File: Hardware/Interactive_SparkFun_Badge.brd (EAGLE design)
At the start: 88.9 x 63.5 mm, 27 parts, among them J1 AVR_SPI_PRG_6NS, U1 ATMEGA328P, Y1 8MHZ

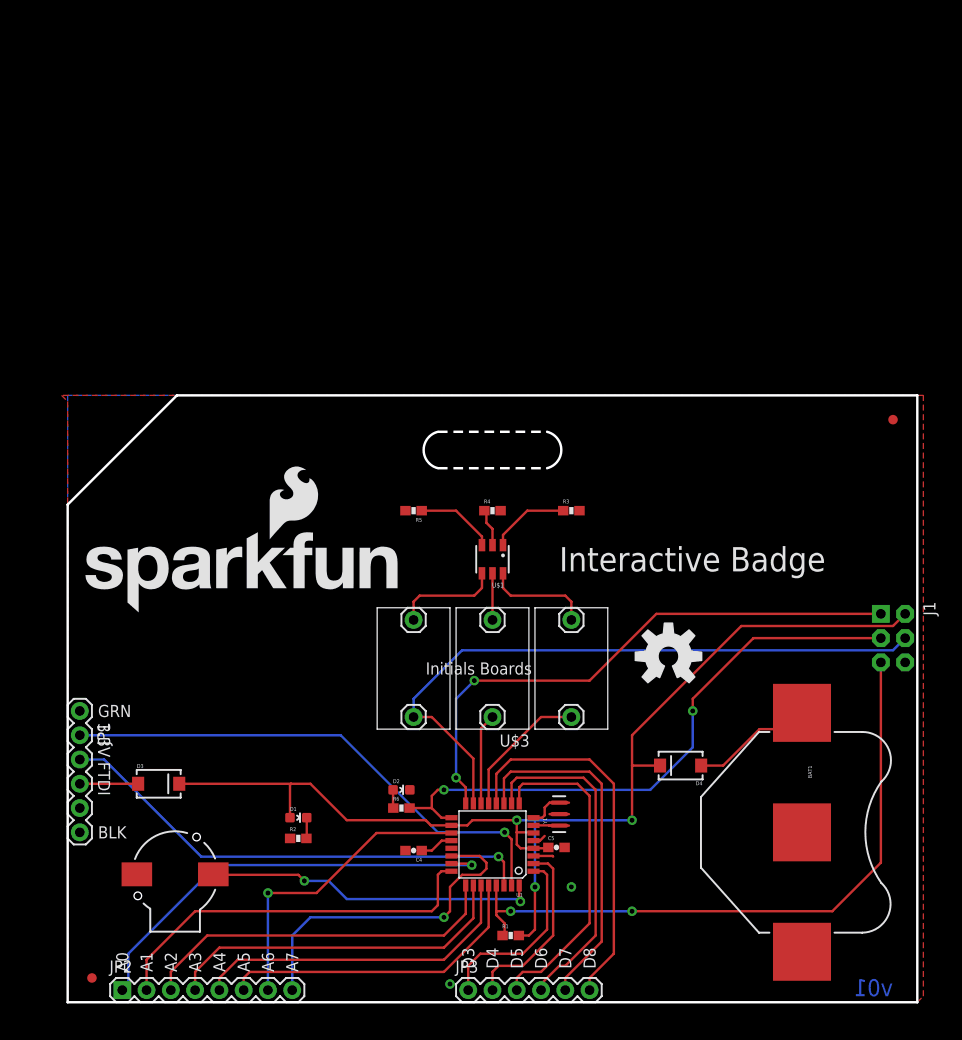
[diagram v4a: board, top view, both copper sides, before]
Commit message: Updating to round corners, zener diodes, larger letter boards
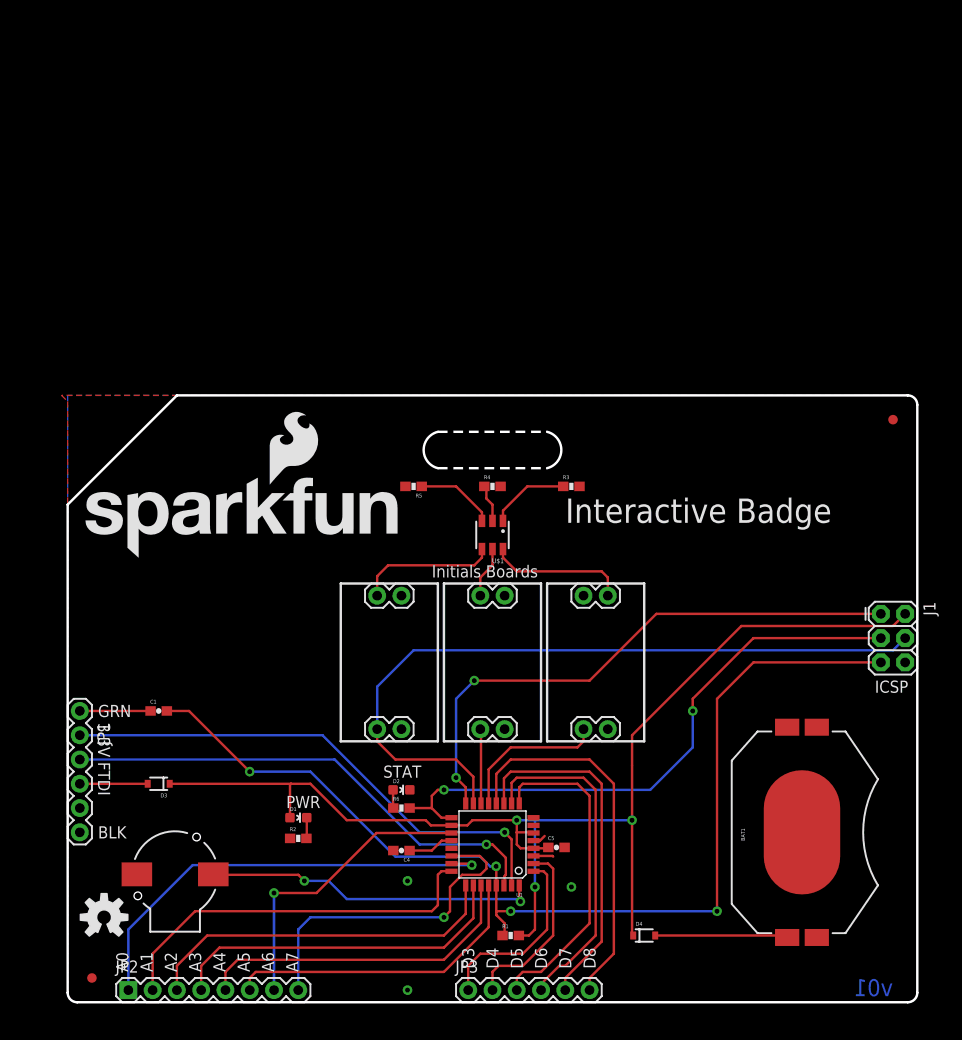
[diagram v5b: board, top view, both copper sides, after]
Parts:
- removed Y1: 8MHZ, SparkFun-FreqCtrl:RESONATOR-SMD
- added C1: 0.1uF, SparkFun-Capacitors:0603-CAP
- BAT1: value (none) -> 20mm coincell; device SparkFun-Electromechanical:BATTCON_20MM -> SparkFun-Electromechanical:BATTCON_20MM_4LEGS
- D3, D4: value MBRA140 -> DIODE-ZENER3.3V; device SparkFun-DiscreteSemi:SMA-DIODE -> SparkFun-DiscreteSemi:SOD-323
- J1: value AVR_SPI_PRG_6NS -> AVR_SPI_PRG_6PTH; device SparkFun-Connectors:2X3-NS -> SparkFun-Connectors:2X3
- LOGO1: value OSHW-LOGOL -> OSHW-LOGOM; device SparkFun-Aesthetics:OSHW-LOGO-L -> SparkFun-Aesthetics:OSHW-LOGO-M
- U$3: value INITIALS_HEADERS -> ALPHABET; device Local Library:INITIALS_HEADERS -> ML8511:INITIALS
- moved LOGO1 65.1 mm to (3.81, 8.89)
- moved D4 18.2 mm to (60.3, 6.99), turned to 0 degrees
- moved U$3 8.52 mm to (60.3, 43.8)
- moved LOGO2 5.71 mm to (1.27, 46.4)
- moved J1 2.84 mm to (85.1, 40.6)
- moved U$1 2.54 mm to (44.5, 48.9)
- moved R3 2.54 mm to (52.7, 54.0)
- moved R4 2.54 mm to (44.5, 54.0)
- moved R5 2.54 mm to (36.2, 54.0)
- moved C4 1.27 mm to (34.9, 15.9)
- moved JP2 0.63 mm to (6.35, 1.27)
- turned BAT1 to 90 degrees
- turned D3 to 180 degrees
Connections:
- removed net N$2: U1.7, Y1.1
- removed net N$3: U1.8, Y1.3
- net D10: now also U$3.8; no longer U$3.4
- net D9: now also U$3.4; no longer U$3.2
- net DTR: now also C1.1
- net GND: no longer Y1.2
- net GREEN: now also U$3.10; no longer U$3.5
- net MOSI: now also U$3.12; no longer U$3.6
- net RED: now also U$3.6; no longer U$3.3
- net RESET: now also C1.2
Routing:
- net RESET: track 69.0 -> 112.9 mm, vias 2 -> 4
- net VCC: track 119.9 -> 130.0 mm
- net MOSI: track 68.7 -> 77.5 mm
- net DTR: track 0.00 -> 7.41 mm
- net GREEN: track 11.2 -> 14.7 mm
- net BLUE: track 11.2 -> 14.6 mm
- net N$3: track 2.81 -> 0.00 mm
- net D10: track 9.54 -> 7.80 mm
- net N$2: track 1.69 -> 0.00 mm
- net D9: track 14.5 -> 16.0 mm
- net N$8: track 3.54 -> 4.81 mm
- net A0: track 46.1 -> 47.3 mm
- net 3.3V: track 6.11 -> 7.11 mm
- net SCL: track 33.5 -> 32.8 mm
- net A6: track 32.0 -> 31.3 mm
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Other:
- outline, holes or cut-outs redrawn
- board text added: "ICSP"
- board text added: "PWR"
- board text added: "STAT"

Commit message: Updating to new power circuit, and adding front silk
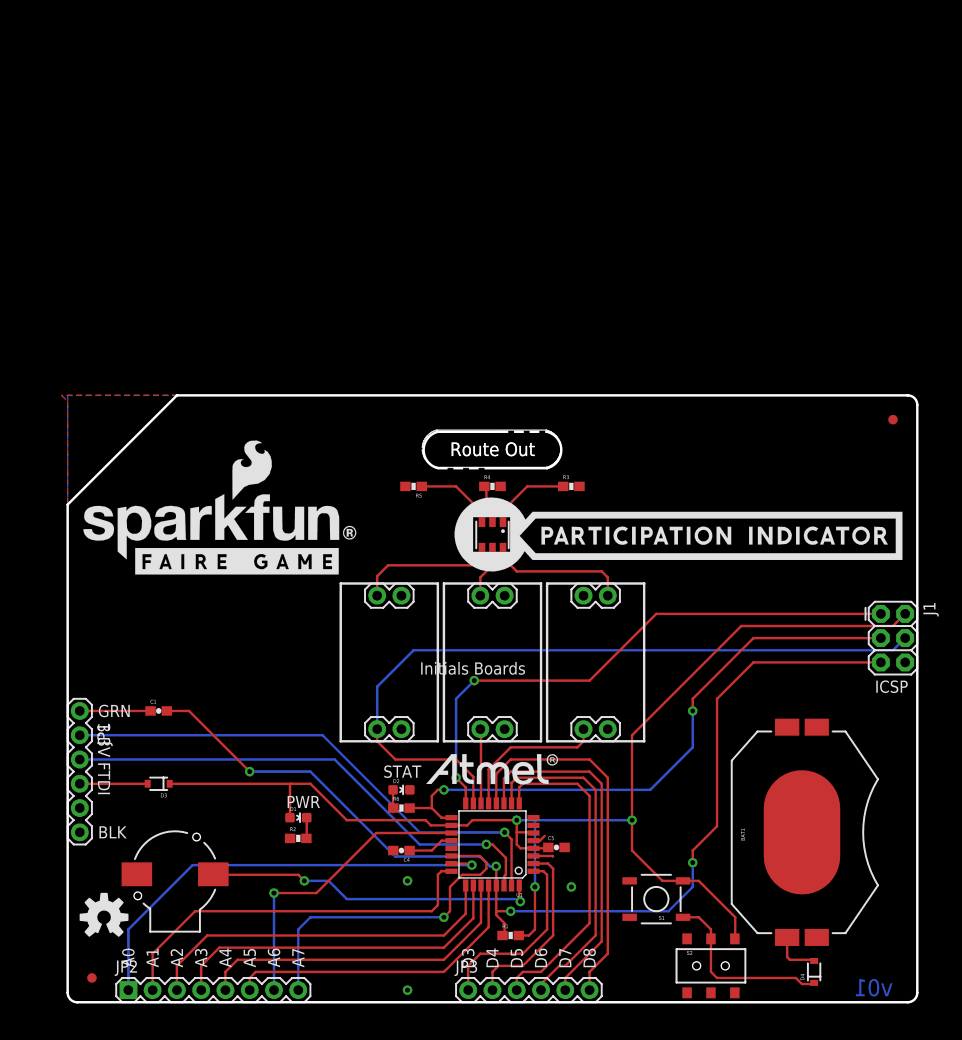
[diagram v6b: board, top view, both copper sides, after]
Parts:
- removed LOGO2: SFE_LOGO_NAME_FLAME.3_INCH, SparkFun-Aesthetics:SFE_LOGO_NAME_FLAME_.3
- added S1: (no value), SparkFun-Electromechanical:TACTILE-SWITCH-SMD
- added S2: (no value), SparkFun-Electromechanical:AYZ0202
- added U$4: FAIRE_GAME_SILK, Local Library:FAIRE_GAME_SILK
- moved D4 18.2 mm to (78.1, 3.17), turned to 90 degrees
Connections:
- new net N$1: D4.C, S1.1, S2.2
- net VCC: now also S1.3, S2.3; no longer D4.C
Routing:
- net N$1: track 0.00 -> 19.3 mm
- net N$10: track 13.9 -> 5.04 mm
- net VCC: track 130.0 -> 137.1 mm
- net RESET: track 112.9 -> 110.0 mm
- net D8: track 39.7 -> 39.2 mm
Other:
- outline, holes or cut-outs redrawn
- board text added: "Route Out"
- board text removed: "Interactive Badge"

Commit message: Adding NY MF silk
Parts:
- added U$2: NY_FAIRE_BACK, Local Library:NY_BACK
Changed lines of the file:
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@@
 <?xml version="1.0" encoding="utf-8"?>
 <!DOCTYPE eagle SYSTEM "eagle.dtd">
-<eagle version="6.5.0">
+<eagle version="6.6.0">
 <drawing>
 <settings>
@@
 <layer number="47" name="Measures" color="7" fill="1" visible="no" active="yes"/>
 <layer number="48" name="Document" color="7" fill="1" visible="no" active="yes"/>
-<layer number="49" name="Reference" color="7" fill="1" visible="no" active="yes"/>
+<layer number="49" name="Reference" color="7" fill="1" visible="yes" active="yes"/>
 <layer number="50" name="dxf" color="7" fill="1" visible="no" active="no"/>
 <layer number="51" name="tDocu" color="6" fill="1" visible="yes" active="yes"/>
@@
 </element>
 <element name="U$4" library="Local Library" package="FAIRE_GAME_SILK" value="FAIRE_GAME_SILK" x="-0.635" y="-0.762"/>
+<element name="U$2" library="Local Library" package="NY_BACK" value="NY_FAIRE_BACK" x="1.27" y="0"/>
 </elements>
 <signals>
